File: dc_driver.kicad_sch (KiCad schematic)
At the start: 42 parts, among them J10 Conn_01x02, J11 Conn_01x04, J12 Conn_01x02, J13 Conn_01x02, J14 Conn_01x02, J3 Conn_01x04, J4 Conn_01x04, J5 Conn_01x02, J6 Conn_01x02, J7 Conn_01x02, J8 Conn_01x02, J9 Conn_01x02, U2 L298N, U3 L298N, U4 L298N

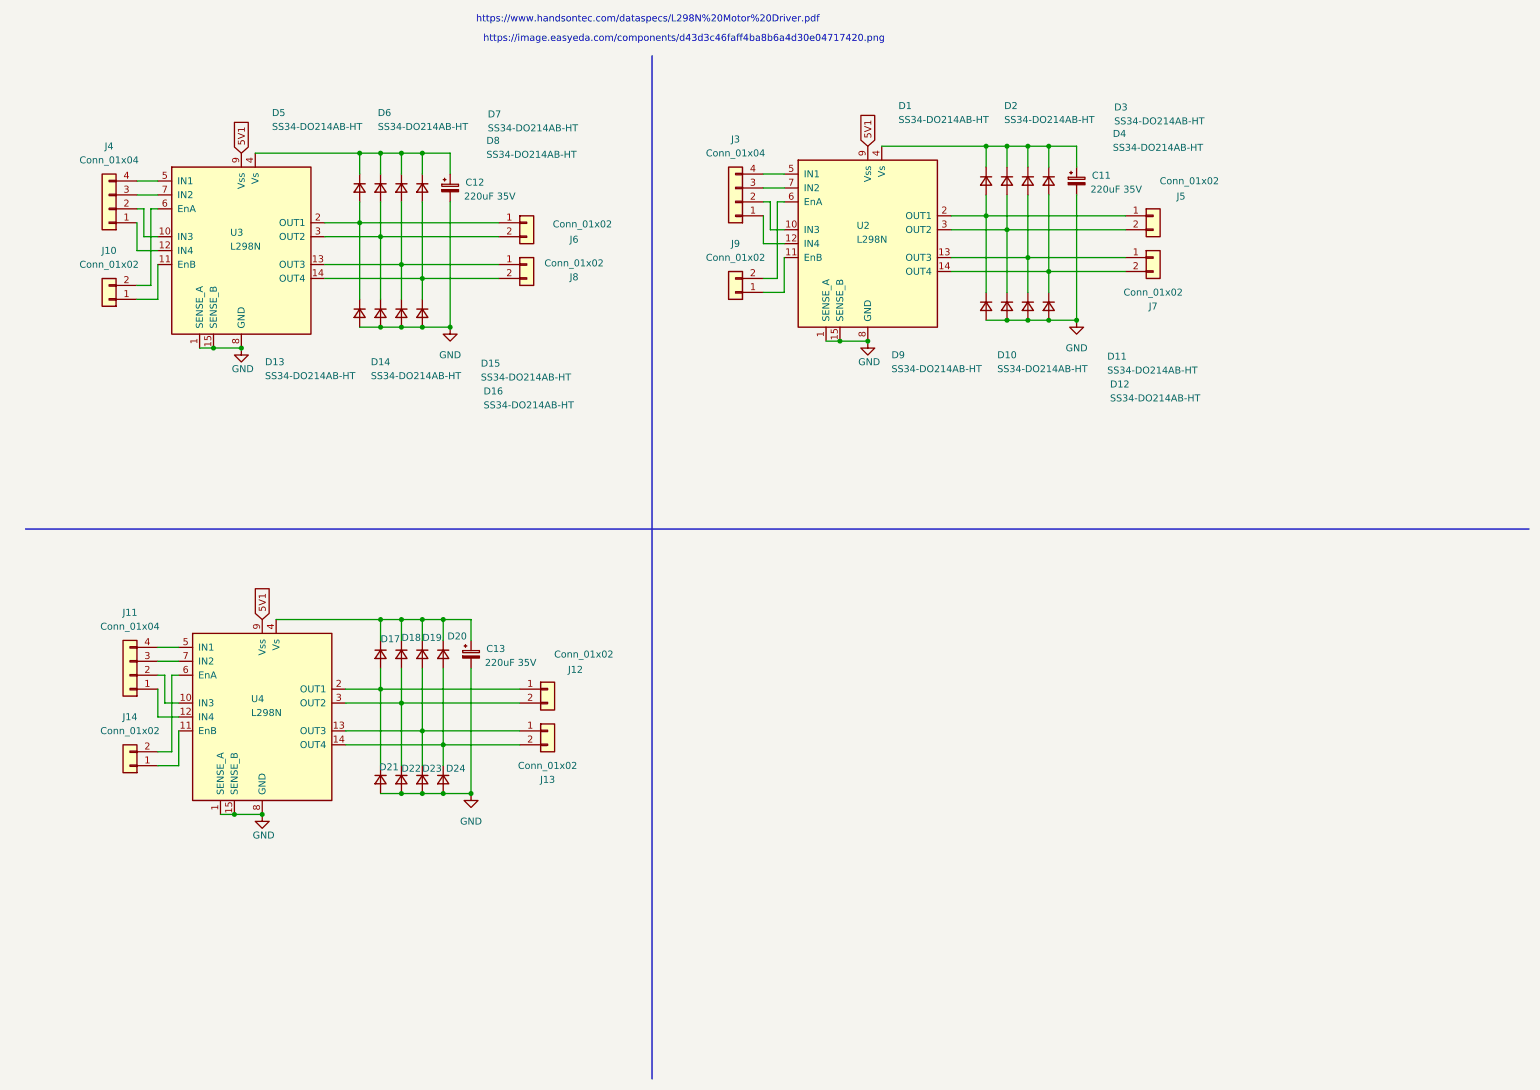
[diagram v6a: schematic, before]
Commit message: some connectors added
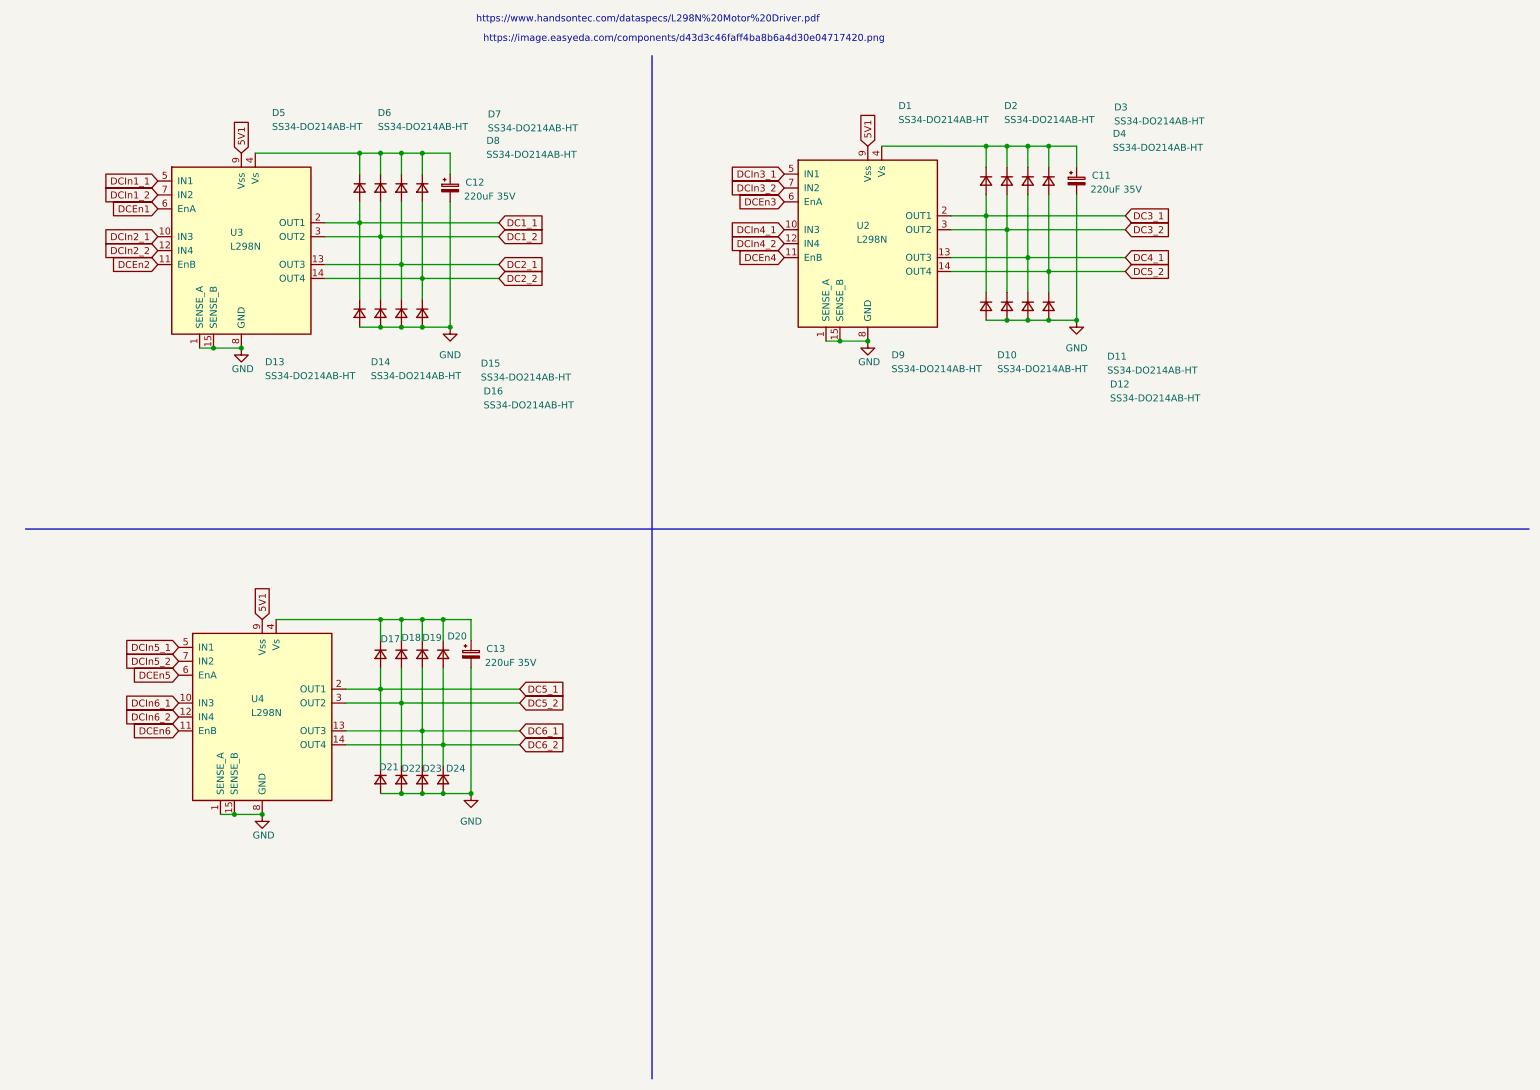
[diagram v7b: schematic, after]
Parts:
- removed J10, J12, J13, J14, J5, J6, J7, J8, J9: Conn_01x02, symbol Connector_Generic:Conn_01x02
- removed J11, J3, J4: Conn_01x04, symbol Connector_Generic:Conn_01x04
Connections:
- net DCIn2_1: now reaches U3.10 (IN3)
- net DCEn2: now reaches U3.11 (EnB)
- net DCIn2_2: now reaches U3.12 (IN4)
- net DC2_1: now reaches D15.1 (K), D7.2 (A), U3.13 (OUT3)
- net DC2_2: now reaches D16.1 (K), D8.2 (A), U3.14 (OUT4)
- net DC1_1: now reaches D13.1 (K), D5.2 (A), U3.2 (OUT1)
- net DC1_2: now reaches D14.1 (K), D6.2 (A), U3.3 (OUT2)
- net DCIn1_1: now reaches U3.5 (IN1)
- net DCEn1: now reaches U3.6 (EnA)
- net DCIn1_2: now reaches U3.7 (IN2)
- net DC6_2: now reaches D20.2 (A), D24.1 (K), U4.14 (OUT4)
- net DC3_1: now reaches D1.2 (A), D9.1 (K), U2.2 (OUT1)
- net DC5_2: now reaches D18.2 (A), D22.1 (K), U4.3 (OUT2)
- net DC5_2: now also D12.1 (K), D4.2 (A), U2.14 (OUT4)
- net DC6_1: now reaches D19.2 (A), D23.1 (K), U4.13 (OUT3)
- net DCIn4_1: now reaches U2.10 (IN3)
- net DCEn4: now reaches U2.11 (EnB)
- net DCIn4_2: now reaches U2.12 (IN4)
- net DC4_1: now reaches D11.1 (K), D3.2 (A), U2.13 (OUT3)
- net DC3_2: now reaches D10.1 (K), D2.2 (A), U2.3 (OUT2)
- net DCIn3_1: now reaches U2.5 (IN1)
- net DCEn3: now reaches U2.6 (EnA)
- net DCIn3_2: now reaches U2.7 (IN2)
- net DCIn6_1: now reaches U4.10 (IN3)
- net DCEn6: now reaches U4.11 (EnB)
- net DCIn6_2: now reaches U4.12 (IN4)
- net DC5_1: now reaches D17.2 (A), D21.1 (K), U4.2 (OUT1)
- net DCIn5_1: now reaches U4.5 (IN1)
- net DCEn5: now reaches U4.6 (EnA)
- net DCIn5_2: now reaches U4.7 (IN2)

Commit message: Visual Improvements
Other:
- note added: "DC Motor Driver 1"
- note added: "DC Motor Driver 2"
- note added: "DC Motor Driver 3"
- moved on the sheet: C11, C12, C13, D1, D10, D11, D12, D13, D14, D15, D16, D17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
